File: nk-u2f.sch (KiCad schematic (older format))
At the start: 25 parts, among them J1 USB_Plug, P1 TouchPAD, U1 EFM8UB30F40G-A, U2 MTCH101, U3 DF5A5.6JE, U4 ATECC508A

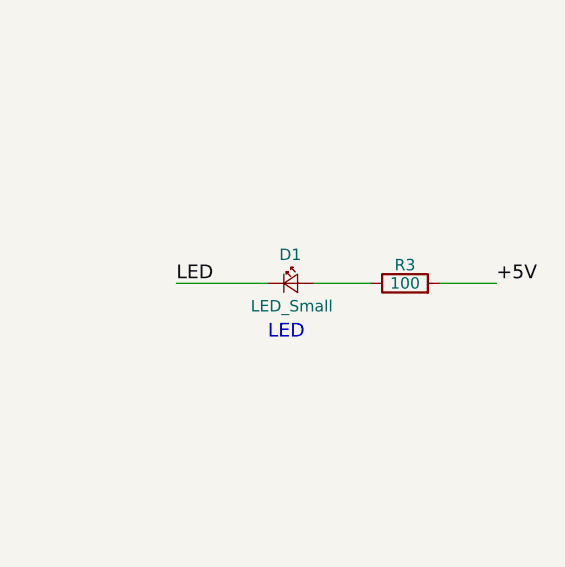
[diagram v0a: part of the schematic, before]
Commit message: Change R3 value 100->390
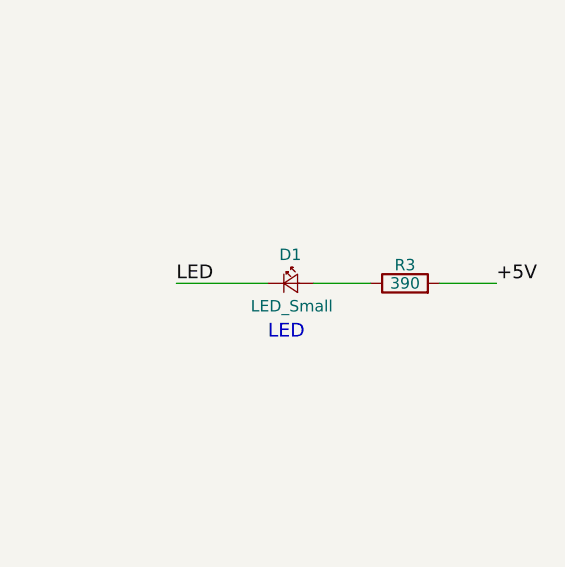
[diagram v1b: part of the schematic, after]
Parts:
- R3: value 100 -> 390
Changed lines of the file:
@@
 P 10300 3950
 F 0 "R3" V 10380 3950 50  0000 C CNN
-F 1 "100" V 10300 3950 50  0000 C CNN
+F 1 "390" V 10300 3950 50  0000 C CNN
 F 2 "Resistors_SMD:R_0402" V 10230 3950 50  0001 C CNN
 F 3 "?" H 10300 3950 50  0001 C CNN

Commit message: R8 with marks, larger touch pad and components moved to backside
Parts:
- C1, C2, C3, C4, C5: symbol nk-u2f-rescue:C -> nk-u2f-rescue:C-nk-u2f-rescue-nk-u2f-rescue
- D1: symbol nk-u2f-rescue:LED_Small -> nk-u2f-rescue:LED_Small-nk-u2f-rescue-nk-u2f-rescue
- J1: symbol nk-u2f-rescue:USB_Plug -> nk-u2f-rescue:USB_Plug-nk-u2f-rescue-nk-u2f-rescue
- P1: symbol nk-u2f-rescue:TouchPAD -> nk-u2f-rescue:TouchPAD-nk-u2f-rescue-nk-u2f-rescue
- R1, R2, R3, R4, R5, R6, R7: symbol nk-u2f-rescue:R -> nk-u2f-rescue:R-nk-u2f-rescue-nk-u2f-rescue
- TP1, TP2, TP3, TP4, TP5, TP6: symbol nk-u2f-rescue:debug-pin -> nk-u2f-rescue:debug-pin-nk-u2f-rescue-nk-u2f-rescue
- U1: symbol nk-u2f-rescue:EFM8UBx-QFN20 -> nk-u2f-rescue:EFM8UBx-QFN20-nk-u2f-rescue-nk-u2f-rescue
- U2: symbol nk-u2f-rescue:MTCH101 -> nk-u2f-rescue:MTCH101-nk-u2f-rescue-nk-u2f-rescue
- U3: symbol nk-u2f-rescue:DF5A5.6JE -> nk-u2f-rescue:DF5A5.6JE-nk-u2f-rescue-nk-u2f-rescue
- U4: symbol nk-u2f-rescue:ATECC508A-RESCUE-u2f-zero -> nk-u2f-rescue:ATECC508A-RESCUE-u2f-zero-nk-u2f-rescue-nk-u2f-rescue
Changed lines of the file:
@@
 Sheet 1 1
 Title "Nitrokey FIDO U2F"
-Date "2018-09-29"
-Rev "R7"
+Date "2019-01-03"
+Rev "R8"
 Comp "Nitrokey"
 Comment1 ""
@@
 $EndDescr
 $Comp
-L nk-u2f-rescue:ATECC508A-RESCUE-u2f-zero U4
+L nk-u2f-rescue:ATECC508A-RESCUE-u2f-zero-nk-u2f-rescue-nk-u2f-rescue U4
 U 1 1 56857313
 P 2100 1350
@@
 +5V
 $Comp
-L nk-u2f-rescue:DF5A5.6JE U3
+L nk-u2f-rescue:DF5A5.6JE-nk-u2f-rescue-nk-u2f-rescue U3
 U 1 1 56857EAF
 P 2400 4150
@@
 HD+
 $Comp
-L nk-u2f-rescue:R R3
+L nk-u2f-rescue:R-nk-u2f-rescue-nk-u2f-rescue R3
 U 1 1 56857B9B
 P 10300 3950
@@
 Secure element for EC
 $Comp
-L nk-u2f-rescue:PWR_FLAG-RESCUE-nk-u2f #FLG01
+L nk-u2f-rescue:PWR_FLAG-RESCUE-nk-u2f-nk-u2f-rescue-nk-u2f-rescue #FLG01
 U 1 1 5686E60B
 P 9650 5800
@@
 C2D
 $Comp
-L nk-u2f-rescue:debug-pin TP5
+L nk-u2f-rescue:debug-pin-nk-u2f-rescue-nk-u2f-rescue TP5
 U 1 1 56A3F8D6
 P 9900 1550
@@
 $EndComp
 $Comp
-L nk-u2f-rescue:debug-pin TP6
+L nk-u2f-rescue:debug-pin-nk-u2f-rescue-nk-u2f-rescue TP6
 U 1 1 56A3F90D
 P 9900 1650
@@
 +5V
 $Comp
-L nk-u2f-rescue:debug-pin TP1
+L nk-u2f-rescue:debug-pin-nk-u2f-rescue-nk-u2f-rescue TP1
 U 1 1 570602D3
 P 9350 1850
@@
 GND
 $Comp
-L nk-u2f-rescue:MTCH101 U2
+L nk-u2f-rescue:MTCH101-nk-u2f-rescue-nk-u2f-rescue U2
 U 1 1 58B45395
 P 6100 1700
@@
 $EndComp
 $Comp
-L nk-u2f-rescue:TouchPAD P1
+L nk-u2f-rescue:TouchPAD-nk-u2f-rescue-nk-u2f-rescue P1
 U 1 1 58B45501
 P 4700 1600
@@
 $EndComp
 $Comp
-L nk-u2f-rescue:R R1
+L nk-u2f-rescue:R-nk-u2f-rescue-nk-u2f-rescue R1
 U 1 1 58B46D59
 P 5350 1600
@@
 Button
 $Comp
-L nk-u2f-rescue:R R2
+L nk-u2f-rescue:R-nk-u2f-rescue-nk-u2f-rescue R2
 U 1 1 58B4B268
 P 5350 1800
@@
 	5200 1800 5100 1800
 $Comp
-L nk-u2f-rescue:C C1
+L nk-u2f-rescue:C-nk-u2f-rescue-nk-u2f-rescue C1
 U 1 1 58B4E061
 P 5100 6500
@@
 	4950 6500 4650 6500
 $Comp
-L nk-u2f-rescue:EFM8UBx-QFN20 U1
+L nk-u2f-rescue:EFM8UBx-QFN20-nk-u2f-rescue-nk-u2f-rescue U1
 U 1 1 58B4B07B
 P 6000 4400
@@
 	2550 5000 2550 4450
 $Comp
-L nk-u2f-rescue:USB_Plug J1
+L nk-u2f-rescue:USB_Plug-nk-u2f-rescue-nk-u2f-rescue J1
 U 1 1 58B4C866
 P 1600 4950
@@
 Maximum Sensitivity\n
 $Comp
-L nk-u2f-rescue:LED_Small D1
+L nk-u2f-rescue:LED_Small-nk-u2f-rescue-nk-u2f-rescue D1
 U 1 1 58BE480C
 P 9800 3950
@@
 GND
 $Comp
-L nk-u2f-rescue:C C2
+L nk-u2f-rescue:C-nk-u2f-rescue-nk-u2f-rescue C2
 U 1 1 58BE8B33
 P 5100 6800
@@
 $EndComp
 $Comp
-L nk-u2f-rescue:C C3
+L nk-u2f-rescue:C-nk-u2f-rescue-nk-u2f-rescue C3
 U 1 1 58BE8F14
 P 5100 7150
@@
 $EndComp
 $Comp
-L nk-u2f-rescue:debug-pin TP3
+L nk-u2f-rescue:debug-pin-nk-u2f-rescue-nk-u2f-rescue TP3
 U 1 1 58BF08D2
 P 9350 2050
@@
 $EndComp
 $Comp
-L nk-u2f-rescue:debug-pin TP2
+L nk-u2f-rescue:debug-pin-nk-u2f-rescue-nk-u2f-rescue TP2
 U 1 1 58BF092E
 P 9350 1950
@@
 HD-
 $Comp
-L nk-u2f-rescue:debug-pin TP4
+L nk-u2f-rescue:debug-pin-nk-u2f-rescue-nk-u2f-rescue TP4
 U 1 1 58BF35A7
 P 9350 2150
@@
 	6750 1700 6750 1050
 $Comp
-L nk-u2f-rescue:R R4
+L nk-u2f-rescue:R-nk-u2f-rescue-nk-u2f-rescue R4
 U 1 1 5A77979E
 P 6450 5400
@@
 +5V
 $Comp
-L nk-u2f-rescue:C C4
+L nk-u2f-rescue:C-nk-u2f-rescue-nk-u2f-rescue C4
 U 1 1 5A779EEC
 P 5100 6200
@@
 Connection ~ 4650 6500
 $Comp
-L nk-u2f-rescue:R R5
+L nk-u2f-rescue:R-nk-u2f-rescue-nk-u2f-rescue R5
 U 1 1 5A77A495
 P 6850 3950
@@
 $EndComp
 $Comp
-L nk-u2f-rescue:R R7
+L nk-u2f-rescue:R-nk-u2f-rescue-nk-u2f-rescue R7
 U 1 1 5A77A548
 P 7050 3950
@@
 +5V
 $Comp
-L nk-u2f-rescue:PWR_FLAG-RESCUE-nk-u2f #FLG02
+L nk-u2f-rescue:PWR_FLAG-RESCUE-nk-u2f-nk-u2f-rescue-nk-u2f-rescue #FLG02
 U 1 1 5A77BCD6
 P 9250 5800
@@
 	7050 4600 7250 4600
 $Comp
-L nk-u2f-rescue:C C5
+L nk-u2f-rescue:C-nk-u2f-rescue-nk-u2f-rescue C5
 U 1 1 5BB01812
 P 1200 5500
@@
 $EndComp
 $Comp
-L nk-u2f-rescue:R R6
+L nk-u2f-rescue:R-nk-u2f-rescue-nk-u2f-rescue R6
 U 1 1 5BB01955
 P 1350 5500

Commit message: R9
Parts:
- C1, C2, C3, C4, C5: symbol nk-u2f-rescue:C-nk-u2f-rescue-nk-u2f-rescue -> nk-u2f-rescue:C-nk-u2f-rescue
- D1: symbol nk-u2f-rescue:LED_Small-nk-u2f-rescue-nk-u2f-rescue -> nk-u2f-rescue:LED_Small-nk-u2f-rescue
- J1: symbol nk-u2f-rescue:USB_Plug-nk-u2f-rescue-nk-u2f-rescue -> nk-u2f-rescue:USB_Plug-nk-u2f-rescue
- P1: symbol nk-u2f-rescue:TouchPAD-nk-u2f-rescue-nk-u2f-rescue -> nk-u2f-rescue:TouchPAD-nk-u2f-rescue
- R1, R2, R3, R4, R5, R6, R7: symbol nk-u2f-rescue:R-nk-u2f-rescue-nk-u2f-rescue -> nk-u2f-rescue:R-nk-u2f-rescue
- TP1, TP2, TP3, TP4, TP5, TP6: symbol nk-u2f-rescue:debug-pin-nk-u2f-rescue-nk-u2f-rescue -> nk-u2f-rescue:debug-pin-nk-u2f-rescue
- U1: symbol nk-u2f-rescue:EFM8UBx-QFN20-nk-u2f-rescue-nk-u2f-rescue -> nk-u2f-rescue:EFM8UBx-QFN20-nk-u2f-rescue
- U2: symbol nk-u2f-rescue:MTCH101-nk-u2f-rescue-nk-u2f-rescue -> nk-u2f-rescue:MTCH101-nk-u2f-rescue
- U3: symbol nk-u2f-rescue:DF5A5.6JE-nk-u2f-rescue-nk-u2f-rescue -> nk-u2f-rescue:DF5A5.6JE-nk-u2f-rescue
- U4: symbol nk-u2f-rescue:ATECC508A-RESCUE-u2f-zero-nk-u2f-rescue-nk-u2f-rescue -> nk-u2f-rescue:ATECC508A-RESCUE-u2f-zero-nk-u2f-rescue
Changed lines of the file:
@@
 Title "Nitrokey FIDO U2F"
 Date "2019-01-03"
-Rev "R8"
+Rev "R9"
 Comp "Nitrokey"
 Comment1 ""
@@
 $EndDescr
 $Comp
-L nk-u2f-rescue:ATECC508A-RESCUE-u2f-zero-nk-u2f-rescue-nk-u2f-rescue U4
+L nk-u2f-rescue:ATECC508A-RESCUE-u2f-zero-nk-u2f-rescue U4
 U 1 1 56857313
 P 2100 1350
@@
 +5V
 $Comp
-L nk-u2f-rescue:DF5A5.6JE-nk-u2f-rescue-nk-u2f-rescue U3
+L nk-u2f-rescue:DF5A5.6JE-nk-u2f-rescue U3
 U 1 1 56857EAF
 P 2400 4150
@@
 HD+
 $Comp
-L nk-u2f-rescue:R-nk-u2f-rescue-nk-u2f-rescue R3
+L nk-u2f-rescue:R-nk-u2f-rescue R3
 U 1 1 56857B9B
 P 10300 3950
@@
 Secure element for EC
 $Comp
-L nk-u2f-rescue:PWR_FLAG-RESCUE-nk-u2f-nk-u2f-rescue-nk-u2f-rescue #FLG01
+L nk-u2f-rescue:PWR_FLAG-RESCUE-nk-u2f-nk-u2f-rescue #FLG01
 U 1 1 5686E60B
 P 9650 5800
@@
 C2D
 $Comp
-L nk-u2f-rescue:debug-pin-nk-u2f-rescue-nk-u2f-rescue TP5
+L nk-u2f-rescue:debug-pin-nk-u2f-rescue TP5
 U 1 1 56A3F8D6
 P 9900 1550
@@
 $EndComp
 $Comp
-L nk-u2f-rescue:debug-pin-nk-u2f-rescue-nk-u2f-rescue TP6
+L nk-u2f-rescue:debug-pin-nk-u2f-rescue TP6
 U 1 1 56A3F90D
 P 9900 1650
@@
 +5V
 $Comp
-L nk-u2f-rescue:debug-pin-nk-u2f-rescue-nk-u2f-rescue TP1
+L nk-u2f-rescue:debug-pin-nk-u2f-rescue TP1
 U 1 1 570602D3
 P 9350 1850
@@
 GND
 $Comp
-L nk-u2f-rescue:MTCH101-nk-u2f-rescue-nk-u2f-rescue U2
+L nk-u2f-rescue:MTCH101-nk-u2f-rescue U2
 U 1 1 58B45395
 P 6100 1700
@@
 $EndComp
 $Comp
-L nk-u2f-rescue:TouchPAD-nk-u2f-rescue-nk-u2f-rescue P1
+L nk-u2f-rescue:TouchPAD-nk-u2f-rescue P1
 U 1 1 58B45501
 P 4700 1600
@@
 $EndComp
 $Comp
-L nk-u2f-rescue:R-nk-u2f-rescue-nk-u2f-rescue R1
+L nk-u2f-rescue:R-nk-u2f-rescue R1
 U 1 1 58B46D59
 P 5350 1600
@@
 Button
 $Comp
-L nk-u2f-rescue:R-nk-u2f-rescue-nk-u2f-rescue R2
+L nk-u2f-rescue:R-nk-u2f-rescue R2
 U 1 1 58B4B268
 P 5350 1800
@@
 	5200 1800 5100 1800
 $Comp
-L nk-u2f-rescue:C-nk-u2f-rescue-nk-u2f-rescue C1
+L nk-u2f-rescue:C-nk-u2f-rescue C1
 U 1 1 58B4E061
 P 5100 6500
@@
 	4950 6500 4650 6500
 $Comp
-L nk-u2f-rescue:EFM8UBx-QFN20-nk-u2f-rescue-nk-u2f-rescue U1
+L nk-u2f-rescue:EFM8UBx-QFN20-nk-u2f-rescue U1
 U 1 1 58B4B07B
 P 6000 4400
@@
 	2550 5000 2550 4450
 $Comp
-L nk-u2f-rescue:USB_Plug-nk-u2f-rescue-nk-u2f-rescue J1
+L nk-u2f-rescue:USB_Plug-nk-u2f-rescue J1
 U 1 1 58B4C866
 P 1600 4950
@@
 Maximum Sensitivity\n
 $Comp
-L nk-u2f-rescue:LED_Small-nk-u2f-rescue-nk-u2f-rescue D1
+L nk-u2f-rescue:LED_Small-nk-u2f-rescue D1
 U 1 1 58BE480C
 P 9800 3950
@@
 GND
 $Comp
-L nk-u2f-rescue:C-nk-u2f-rescue-nk-u2f-rescue C2
+L nk-u2f-rescue:C-nk-u2f-rescue C2
 U 1 1 58BE8B33
 P 5100 6800
@@
 $EndComp
 $Comp
-L nk-u2f-rescue:C-nk-u2f-rescue-nk-u2f-rescue C3
+L nk-u2f-rescue:C-nk-u2f-rescue C3
 U 1 1 58BE8F14
 P 5100 7150
@@
 $EndComp
 $Comp
-L nk-u2f-rescue:debug-pin-nk-u2f-rescue-nk-u2f-rescue TP3
+L nk-u2f-rescue:debug-pin-nk-u2f-rescue TP3
 U 1 1 58BF08D2
 P 9350 2050
@@
 $EndComp
 $Comp
-L nk-u2f-rescue:debug-pin-nk-u2f-rescue-nk-u2f-rescue TP2
+L nk-u2f-rescue:debug-pin-nk-u2f-rescue TP2
 U 1 1 58BF092E
 P 9350 1950
@@
 HD-
 $Comp
-L nk-u2f-rescue:debug-pin-nk-u2f-rescue-nk-u2f-rescue TP4
+L nk-u2f-rescue:debug-pin-nk-u2f-rescue TP4
 U 1 1 58BF35A7
 P 9350 2150
@@
 	6750 1700 6750 1050
 $Comp
-L nk-u2f-rescue:R-nk-u2f-rescue-nk-u2f-rescue R4
+L nk-u2f-rescue:R-nk-u2f-rescue R4
 U 1 1 5A77979E
 P 6450 5400
@@
 +5V
 $Comp
-L nk-u2f-rescue:C-nk-u2f-rescue-nk-u2f-rescue C4
+L nk-u2f-rescue:C-nk-u2f-rescue C4
 U 1 1 5A779EEC
 P 5100 6200
@@
 Connection ~ 4650 6500
 $Comp
-L nk-u2f-rescue:R-nk-u2f-rescue-nk-u2f-rescue R5
+L nk-u2f-rescue:R-nk-u2f-rescue R5
 U 1 1 5A77A495
 P 6850 3950
@@
 $EndComp
 $Comp
-L nk-u2f-rescue:R-nk-u2f-rescue-nk-u2f-rescue R7
+L nk-u2f-rescue:R-nk-u2f-rescue R7
 U 1 1 5A77A548
 P 7050 3950
@@
 +5V
 $Comp
-L nk-u2f-rescue:PWR_FLAG-RESCUE-nk-u2f-nk-u2f-rescue-nk-u2f-rescue #FLG02
+L nk-u2f-rescue:PWR_FLAG-RESCUE-nk-u2f-nk-u2f-rescue #FLG02
 U 1 1 5A77BCD6
 P 9250 5800
@@
 	7050 4600 7250 4600
 $Comp
-L nk-u2f-rescue:C-nk-u2f-rescue-nk-u2f-rescue C5
+L nk-u2f-rescue:C-nk-u2f-rescue C5
 U 1 1 5BB01812
 P 1200 5500
@@
 $EndComp
 $Comp
-L nk-u2f-rescue:R-nk-u2f-rescue-nk-u2f-rescue R6
+L nk-u2f-rescue:R-nk-u2f-rescue R6
 U 1 1 5BB01955
 P 1350 5500
